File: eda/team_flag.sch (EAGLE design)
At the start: 18 parts, among them Q1 MOSFET-LOGIC-NCHANNELSMD, Q2 MOSFET-LOGIC-NCHANNELSMD, U1 ISL83491SOIC, U2 ATTINY1634

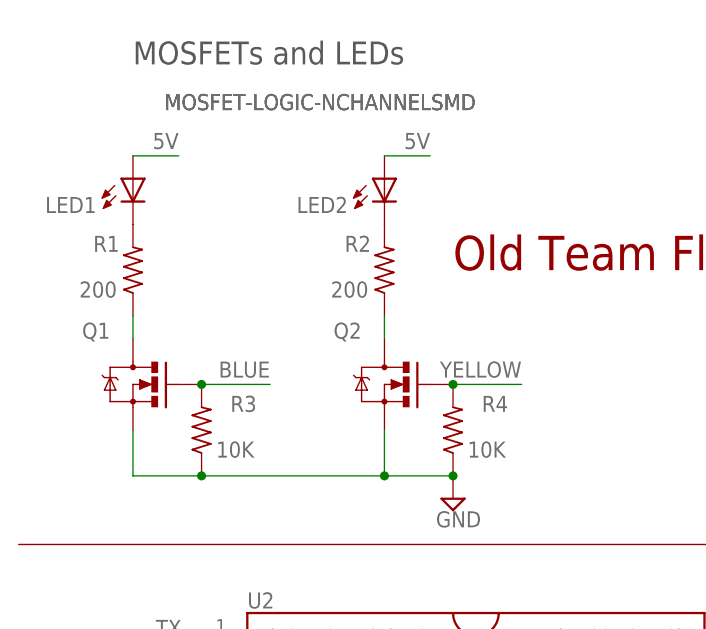
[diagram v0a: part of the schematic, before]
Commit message: Add some BOM metadata
* SMA-package diodes
* SOT23-3 MOSFETs
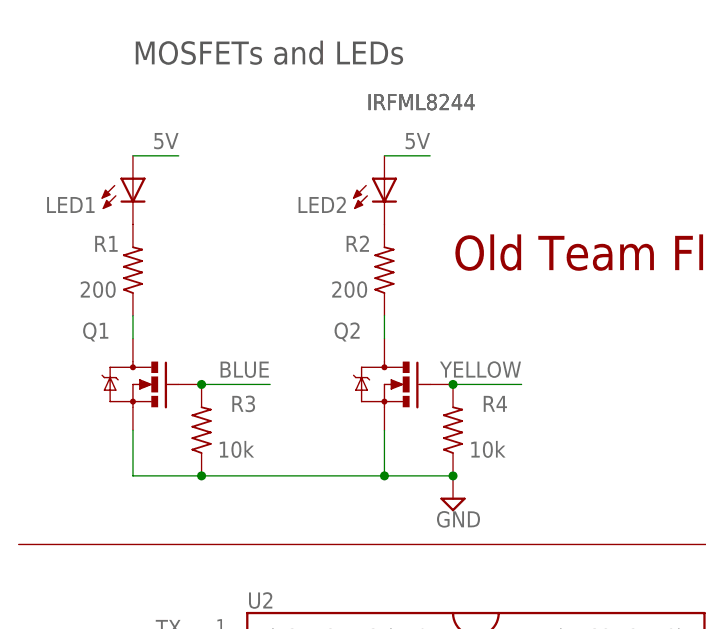
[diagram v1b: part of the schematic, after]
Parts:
- Q1, Q2: value MOSFET-LOGIC-NCHANNELSMD -> IRFML8244; device pie:MOSFET-LOGIC-NCHANNELSMD -> pie:MOSFET-NCHANNELSMD
- R3, R4: value 10K -> 10k
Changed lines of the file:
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@@
 <part name="R1" library="rcl" deviceset="R-US_" device="R0603" value="200"/>
 <part name="R2" library="rcl" deviceset="R-US_" device="R0603" value="200"/>
-<part name="Q1" library="pie" deviceset="MOSFET-LOGIC-NCHANNEL" device="SMD"/>
-<part name="Q2" library="pie" deviceset="MOSFET-LOGIC-NCHANNEL" device="SMD"/>
+<part name="Q1" library="pie" deviceset="MOSFET-NCHANNEL" device="SMD" value="IRFML8244"/>
+<part name="Q2" library="pie" deviceset="MOSFET-NCHANNEL" device="SMD" value="IRFML8244"/>
 <part name="SUPPLY1" library="pie" deviceset="GND" device=""/>
 <part name="FRAME1" library="pie" deviceset="FRAME-LETTER" device="">
@@
 <attribute name="REVISION" value="C"/>
 </part>
-<part name="R3" library="rcl" deviceset="R-US_" device="R0603" value="10K"/>
-<part name="R4" library="rcl" deviceset="R-US_" device="R0603" value="10K"/>
+<part name="R3" library="rcl" deviceset="R-US_" device="R0603" value="10k"/>
+<part name="R4" library="rcl" deviceset="R-US_" device="R0603" value="10k"/>
 <part name="U1" library="pie" deviceset="ISL83491" device="SOIC"/>
 <part name="U2" library="pie" deviceset="ATTINY1634" device=""/>

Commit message: Fix having/not having space in part values; add misc resistors
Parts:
- R3, R4: device rcl:R-US_R0603 -> pie:R-US_R0603
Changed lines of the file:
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@@
 <attribute name="REVISION" value="C"/>
 </part>
-<part name="R3" library="rcl" deviceset="R-US_" device="R0603" value="10k"/>
-<part name="R4" library="rcl" deviceset="R-US_" device="R0603" value="10k"/>
+<part name="R3" library="pie" deviceset="R-US_" device="R0603" value="10k"/>
+<part name="R4" library="pie" deviceset="R-US_" device="R0603" value="10k"/>
 <part name="U1" library="pie" deviceset="ISL83491" device="SOIC"/>
 <part name="U2" library="pie" deviceset="ATTINY1634" device=""/>

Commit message: Update a bunch more part metadata
Team flag, smartsensor jig, both smartsensors, and controller now have
complete BOM information.
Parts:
- LED1: value (none) -> BLUE
- LED2: value (none) -> YELLOW
- R1, R2: device rcl:R-US_R0603 -> pie:R-US_R0603
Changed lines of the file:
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@@
 </classes>
 <parts>
-<part name="LED1" library="pie" deviceset="LED" device="LED5MM-NOFLAT"/>
-<part name="LED2" library="pie" deviceset="LED" device="LED5MM-NOFLAT"/>
-<part name="R1" library="rcl" deviceset="R-US_" device="R0603" value="200"/>
-<part name="R2" library="rcl" deviceset="R-US_" device="R0603" value="200"/>
+<part name="LED1" library="pie" deviceset="LED" device="LED5MM-NOFLAT" value="BLUE"/>
+<part name="LED2" library="pie" deviceset="LED" device="LED5MM-NOFLAT" value="YELLOW"/>
+<part name="R1" library="pie" deviceset="R-US_" device="R0603" value="200"/>
+<part name="R2" library="pie" deviceset="R-US_" device="R0603" value="200"/>
 <part name="Q1" library="pie" deviceset="MOSFET-NCHANNEL" device="SMD" value="IRFML8244"/>
 <part name="Q2" library="pie" deviceset="MOSFET-NCHANNEL" device="SMD" value="IRFML8244"/>

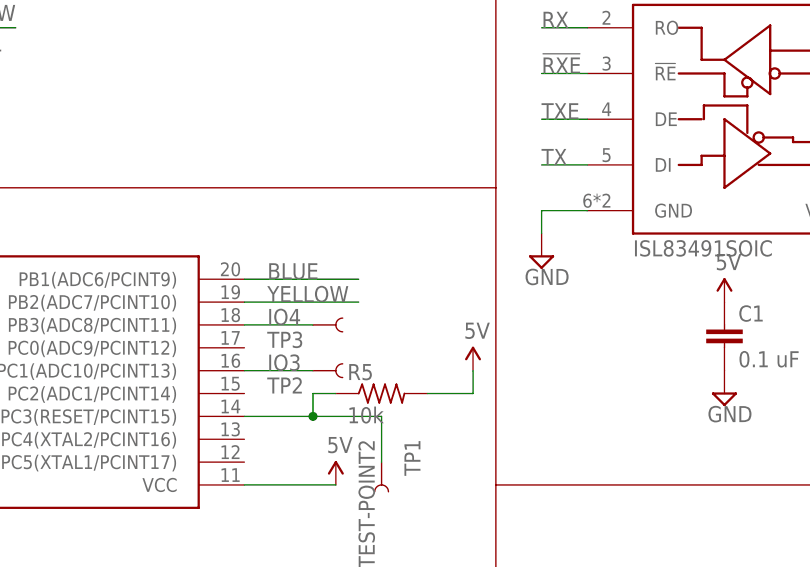
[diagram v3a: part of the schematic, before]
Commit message: Made battery_buzzer_jig and team_flag_jig.
battery_buzzer_jig incomplete.

Test points added to team flag for the jig
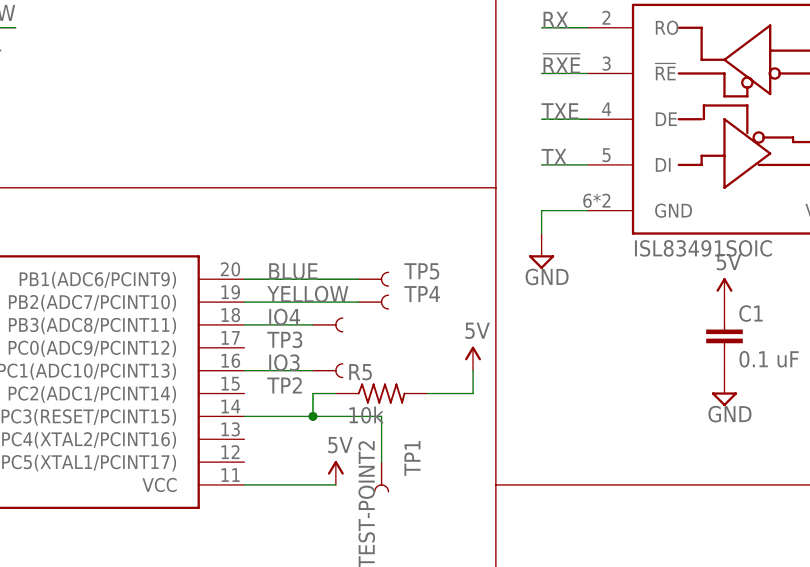
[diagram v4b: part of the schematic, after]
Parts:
- added TP4, TP5: TEST-POINT2, pie:TEST-POINT2
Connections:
- net BLUE: now also TP5.1
- net YELLOW: now also TP4.1
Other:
- note added: "TP4"
- note added: "TP5"
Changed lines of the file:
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@@
 <setting verticaltext="up"/>
 </settings>
-<grid distance="0.1" unitdist="inch" unit="inch" style="lines" multiple="1" display="yes" altdistance="0.05" altunitdist="inch" altunit="inch"/>
+<grid distance="0.1" unitdist="inch" unit="inch" style="lines" multiple="1" display="no" altdistance="0.01" altunitdist="inch" altunit="inch"/>
 <layers>
 <layer number="1" name="Top" color="4" fill="1" visible="no" active="no"/>
@@
 <part name="TP2" library="pie" deviceset="TEST-POINT" device="2" value="IO3"/>
 <part name="TP3" library="pie" deviceset="TEST-POINT" device="2" value="IO4"/>
+<part name="TP4" library="pie" deviceset="TEST-POINT" device="2"/>
+<part name="TP5" library="pie" deviceset="TEST-POINT" device="2"/>
 </parts>
 <sheets>
@@
 <wire x1="0" y1="78.74" x2="109.22" y2="78.74" width="0.1524" layer="94"/>
 <wire x1="109.22" y1="78.74" x2="109.22" y2="93.98" width="0.1524" layer="94"/>
+<text x="99.06" y="114.3" size="1.778" layer="95">TP4</text>
+<text x="99.06" y="116.84" size="1.778" layer="95">TP5</text>
 </plain>
 <instances>
@@
 <attribute name="NAME" x="83.82" y="109.22" size="1.778" layer="95"/>
 </instance>
+<instance part="TP4" gate="G$1" x="93.98" y="114.3" smashed="yes"/>
+<instance part="TP5" gate="G$1" x="93.98" y="116.84" smashed="yes"/>
 </instances>
 <busses>
@@
 <wire x1="81.28" y1="114.3" x2="93.98" y2="114.3" width="0.1524" layer="91"/>
 <label x="83.82" y="114.3" size="1.778" layer="95"/>
+<pinref part="TP4" gate="G$1" pin="1"/>
 </segment>
 </net>
@@
 <wire x1="81.28" y1="116.84" x2="93.98" y2="116.84" width="0.1524" layer="91"/>
 <label x="83.82" y="116.84" size="1.778" layer="95"/>
+<pinref part="TP5" gate="G$1" pin="1"/>
 </segment>
 </net>

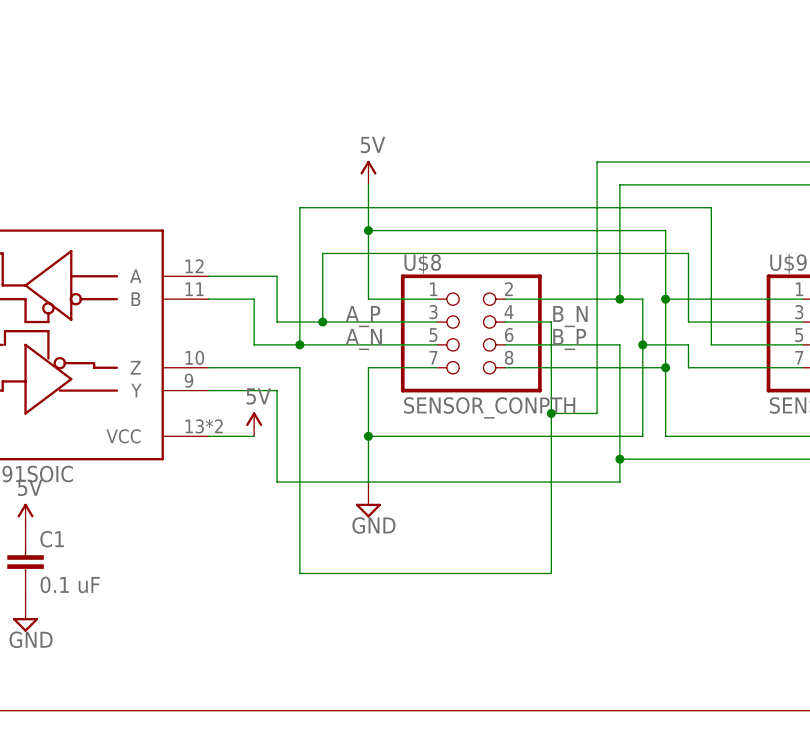
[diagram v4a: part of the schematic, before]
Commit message: Update all smart-sensor protocol boards to use new pinout
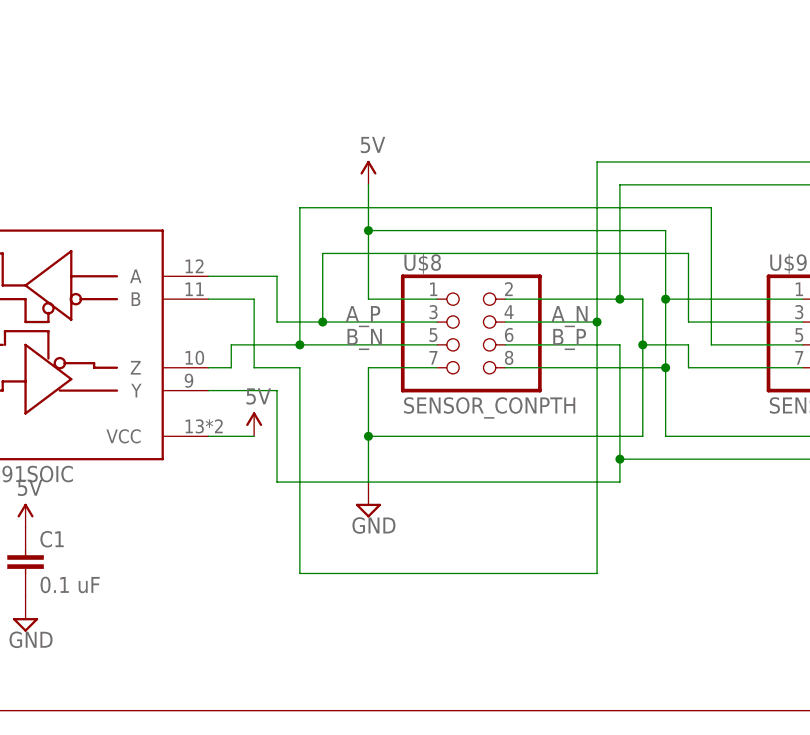
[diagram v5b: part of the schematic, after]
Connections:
- net A_N: now also U$8.4, U$9.4; no longer U$8.5, U$9.5
- net B_N: now also U$8.5, U$9.5; no longer U$8.4, U$9.4
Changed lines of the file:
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@@
 </segment>
 </net>
-<net name="A_N" class="0">
+<net name="B_N" class="0">
 <segment>
 <pinref part="U$8" gate="G$1" pin="5"/>
 <wire x1="180.34" y1="134.62" x2="165.1" y2="134.62" width="0.1524" layer="91"/>
-<wire x1="165.1" y1="134.62" x2="160.02" y2="134.62" width="0.1524" layer="91"/>
-<wire x1="160.02" y1="134.62" x2="160.02" y2="139.7" width="0.1524" layer="91"/>
-<pinref part="U1" gate="G$1" pin="B"/>
-<wire x1="160.02" y1="139.7" x2="154.94" y2="139.7" width="0.1524" layer="91"/>
 <label x="170.18" y="134.62" size="1.778" layer="95"/>
 <pinref part="U$9" gate="G$1" pin="5"/>
@@
 <wire x1="165.1" y1="149.86" x2="165.1" y2="134.62" width="0.1524" layer="91"/>
 <junction x="165.1" y="134.62"/>
+<pinref part="U1" gate="G$1" pin="Z"/>
+<wire x1="165.1" y1="134.62" x2="157.48" y2="134.62" width="0.1524" layer="91"/>
+<wire x1="157.48" y1="134.62" x2="157.48" y2="132.08" width="0.1524" layer="91"/>
+<wire x1="157.48" y1="132.08" x2="154.94" y2="132.08" width="0.1524" layer="91"/>
 </segment>
 </net>
-<net name="B_N" class="0">
+<net name="A_N" class="0">
 <segment>
 <pinref part="U$8" gate="G$1" pin="4"/>
-<wire x1="187.96" y1="137.16" x2="193.04" y2="137.16" width="0.1524" layer="91"/>
-<wire x1="193.04" y1="137.16" x2="193.04" y2="127" width="0.1524" layer="91"/>
-<wire x1="193.04" y1="127" x2="193.04" y2="109.22" width="0.1524" layer="91"/>
-<wire x1="193.04" y1="109.22" x2="165.1" y2="109.22" width="0.1524" layer="91"/>
+<wire x1="187.96" y1="137.16" x2="198.12" y2="137.16" width="0.1524" layer="91"/>
+<wire x1="198.12" y1="137.16" x2="198.12" y2="109.22" width="0.1524" layer="91"/>
+<wire x1="198.12" y1="109.22" x2="165.1" y2="109.22" width="0.1524" layer="91"/>
 <wire x1="165.1" y1="109.22" x2="165.1" y2="132.08" width="0.1524" layer="91"/>
-<pinref part="U1" gate="G$1" pin="Z"/>
-<wire x1="165.1" y1="132.08" x2="154.94" y2="132.08" width="0.1524" layer="91"/>
 <label x="193.04" y="137.16" size="1.778" layer="95"/>
 <pinref part="U$9" gate="G$1" pin="4"/>
@@
 <wire x1="236.22" y1="137.16" x2="236.22" y2="154.94" width="0.1524" layer="91"/>
 <wire x1="236.22" y1="154.94" x2="198.12" y2="154.94" width="0.1524" layer="91"/>
-<wire x1="198.12" y1="154.94" x2="198.12" y2="127" width="0.1524" layer="91"/>
-<wire x1="198.12" y1="127" x2="193.04" y2="127" width="0.1524" layer="91"/>
-<junction x="193.04" y="127"/>
+<wire x1="198.12" y1="154.94" x2="198.12" y2="137.16" width="0.1524" layer="91"/>
+<junction x="198.12" y="137.16"/>
+<pinref part="U1" gate="G$1" pin="B"/>
+<wire x1="154.94" y1="139.7" x2="160.02" y2="139.7" width="0.1524" layer="91"/>
+<wire x1="160.02" y1="139.7" x2="160.02" y2="132.08" width="0.1524" layer="91"/>
+<wire x1="160.02" y1="132.08" x2="165.1" y2="132.08" width="0.1524" layer="91"/>
 </segment>
 </net>

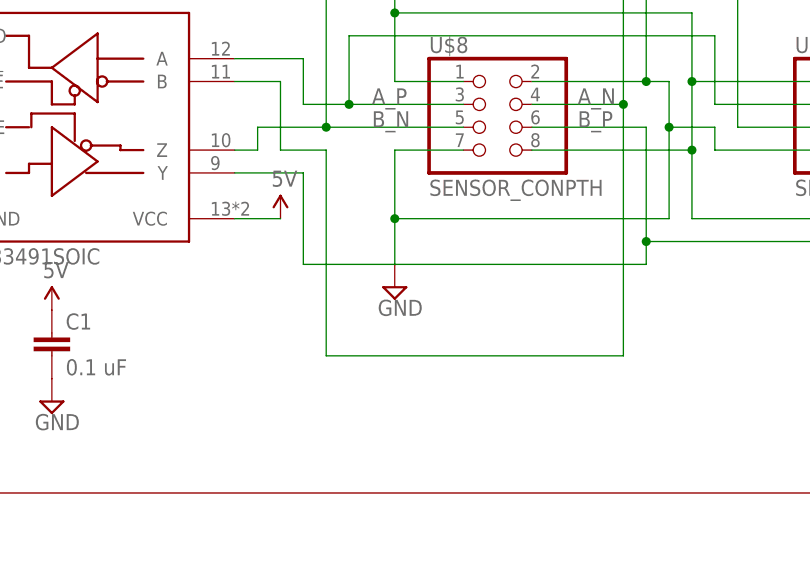
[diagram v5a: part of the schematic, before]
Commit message: Tiny fixes to team_flag, battery_buzzer, and respective jigs.
To all of them:
- silkscreen font reformatting.
- date in copper layer changed/added.

Board specific:
- team_flag:  test points repositioned.
- team_flag_jig:  test points repositioned; version code added.
- battery_buzzer:  version code added; part values added.
- battery_buzzer_jig:  version code added.
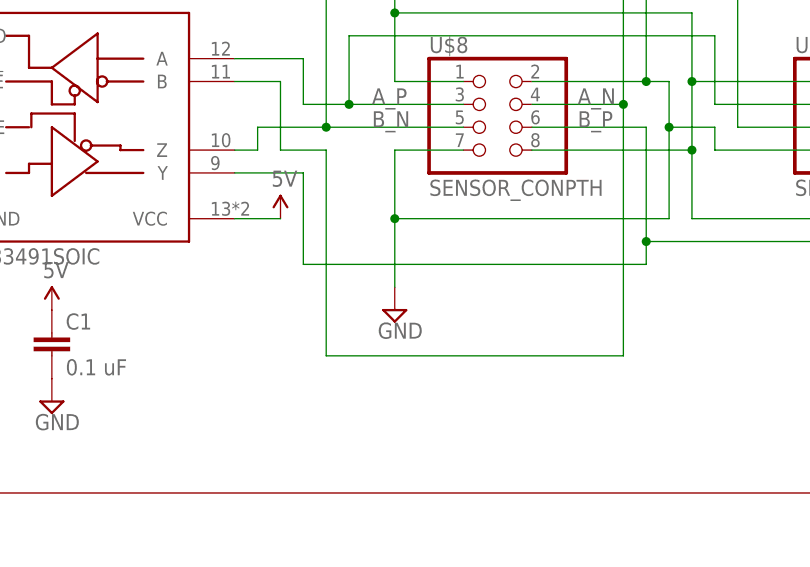
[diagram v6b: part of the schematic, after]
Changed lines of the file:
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@@
 <instance part="U$9" gate="G$1" x="226.06" y="137.16"/>
 <instance part="U$10" gate="G$1" x="172.72" y="152.4"/>
-<instance part="SUPPLY6" gate="GND" x="172.72" y="116.84"/>
+<instance part="SUPPLY6" gate="GND" x="172.72" y="114.3"/>
 <instance part="TP1" gate="G$1" x="96.52" y="96.52" rot="R270"/>
 <instance part="FRAME1" gate="G$1" x="0" y="0"/>
@@
 <wire x1="172.72" y1="132.08" x2="172.72" y2="124.46" width="0.1524" layer="91"/>
 <pinref part="U$8" gate="G$1" pin="2"/>
-<wire x1="172.72" y1="124.46" x2="172.72" y2="119.38" width="0.1524" layer="91"/>
+<wire x1="172.72" y1="124.46" x2="172.72" y2="116.84" width="0.1524" layer="91"/>
 <wire x1="187.96" y1="139.7" x2="200.66" y2="139.7" width="0.1524" layer="91"/>
 <wire x1="200.66" y1="139.7" x2="203.2" y2="139.7" width="0.1524" layer="91"/>

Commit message: Much tidying in pie.lbr
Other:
- moved on the sheet: C1, C2, LED1, LED2
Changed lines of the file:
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@@
 <setting verticaltext="up"/>
 </settings>
-<grid distance="0.1" unitdist="inch" unit="inch" style="lines" multiple="1" display="no" altdistance="0.01" altunitdist="inch" altunit="inch"/>
+<grid distance="0.1" unitdist="inch" unit="inch" style="lines" multiple="1" display="yes" altdistance="0.01" altunitdist="inch" altunit="inch"/>
 <layers>
 <layer number="1" name="Top" color="4" fill="1" visible="no" active="no"/>
@@
 </plain>
 <instances>
-<instance part="LED1" gate="G$1" x="12.7" y="165.1" smashed="yes">
-<attribute name="NAME" x="8.636" y="165.608" size="1.778" layer="95" rot="R180"/>
-<attribute name="VALUE" x="18.415" y="160.528" size="1.778" layer="96" rot="R90"/>
-</instance>
-<instance part="LED2" gate="G$1" x="40.64" y="165.1" smashed="yes">
-<attribute name="NAME" x="36.576" y="165.608" size="1.778" layer="95" rot="R180"/>
-<attribute name="VALUE" x="46.355" y="160.528" size="1.778" layer="96" rot="R90"/>
+<instance part="LED1" gate="G$1" x="12.7" y="166.37" smashed="yes" rot="R270">
+<attribute name="NAME" x="15.24" y="165.1" size="1.778" layer="95"/>
+<attribute name="VALUE" x="15.24" y="162.56" size="1.778" layer="96"/>
+</instance>
+<instance part="LED2" gate="G$1" x="40.64" y="166.37" smashed="yes" rot="R270">
+<attribute name="NAME" x="43.18" y="165.1" size="1.778" layer="95"/>
+<attribute name="VALUE" x="43.18" y="162.56" size="1.778" layer="96"/>
 </instance>
 <instance part="R1" gate="G$1" x="12.7" y="157.48" smashed="yes" rot="R90">
@@
 <instance part="SUPPLY2" gate="GND" x="15.24" y="88.9"/>
 <instance part="SUPPLY3" gate="GND" x="114.3" y="119.38"/>
-<instance part="C1" gate="G$1" x="134.62" y="109.22"/>
-<instance part="C2" gate="G$1" x="5.08" y="93.98"/>
-<instance part="U$5" gate="G$1" x="134.62" y="114.3"/>
+<instance part="C1" gate="G$1" x="134.62" y="109.22" smashed="yes" rot="R270">
+<attribute name="NAME" x="135.89" y="109.22" size="1.778" layer="95"/>
+<attribute name="VALUE" x="135.89" y="104.14" size="1.778" layer="96"/>
+</instance>
+<instance part="C2" gate="G$1" x="5.08" y="96.52" smashed="yes" rot="R270">
+<attribute name="NAME" x="6.35" y="96.52" size="1.778" layer="95"/>
+<attribute name="VALUE" x="6.35" y="91.44" size="1.778" layer="96"/>
+</instance>
+<instance part="U$5" gate="G$1" x="134.62" y="111.76"/>
 <instance part="U$6" gate="G$1" x="5.08" y="99.06"/>
 <instance part="SUPPLY4" gate="GND" x="5.08" y="88.9"/>
-<instance part="SUPPLY5" gate="GND" x="134.62" y="104.14"/>
+<instance part="SUPPLY5" gate="GND" x="134.62" y="101.6"/>
 <instance part="R5" gate="G$1" x="96.52" y="104.14"/>
 <instance part="U$7" gate="G$1" x="106.68" y="106.68"/>
